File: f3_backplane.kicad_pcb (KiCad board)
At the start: 4 copper layers, 95.8 x 73.8 mm, 47 parts, among them J1 PCIEx4_HOST, J2 Bus_M.2_Socket_M, J3 SATA_Backplane, J4 SATA_Backplane, U1 NCP45521, U2 NCP45521, U3 NCP45521, U4 NCP45521

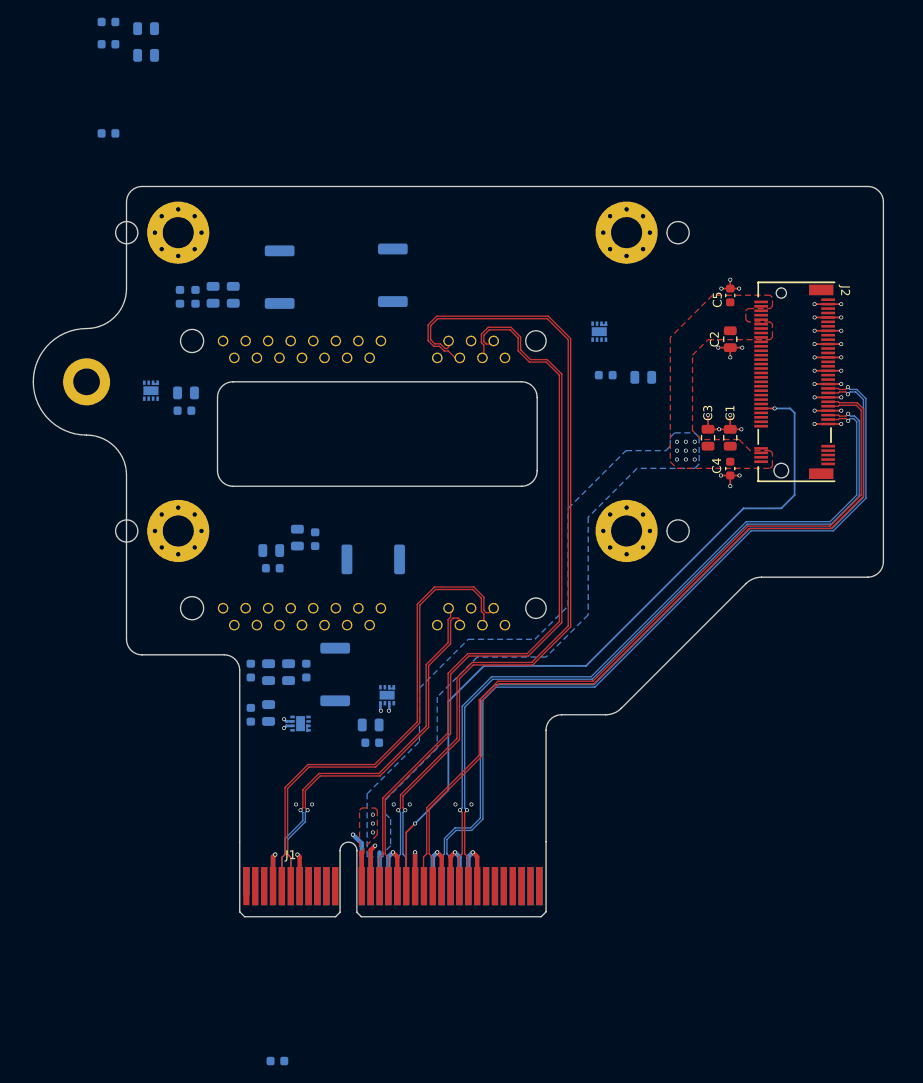
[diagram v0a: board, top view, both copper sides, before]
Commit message: Routing power
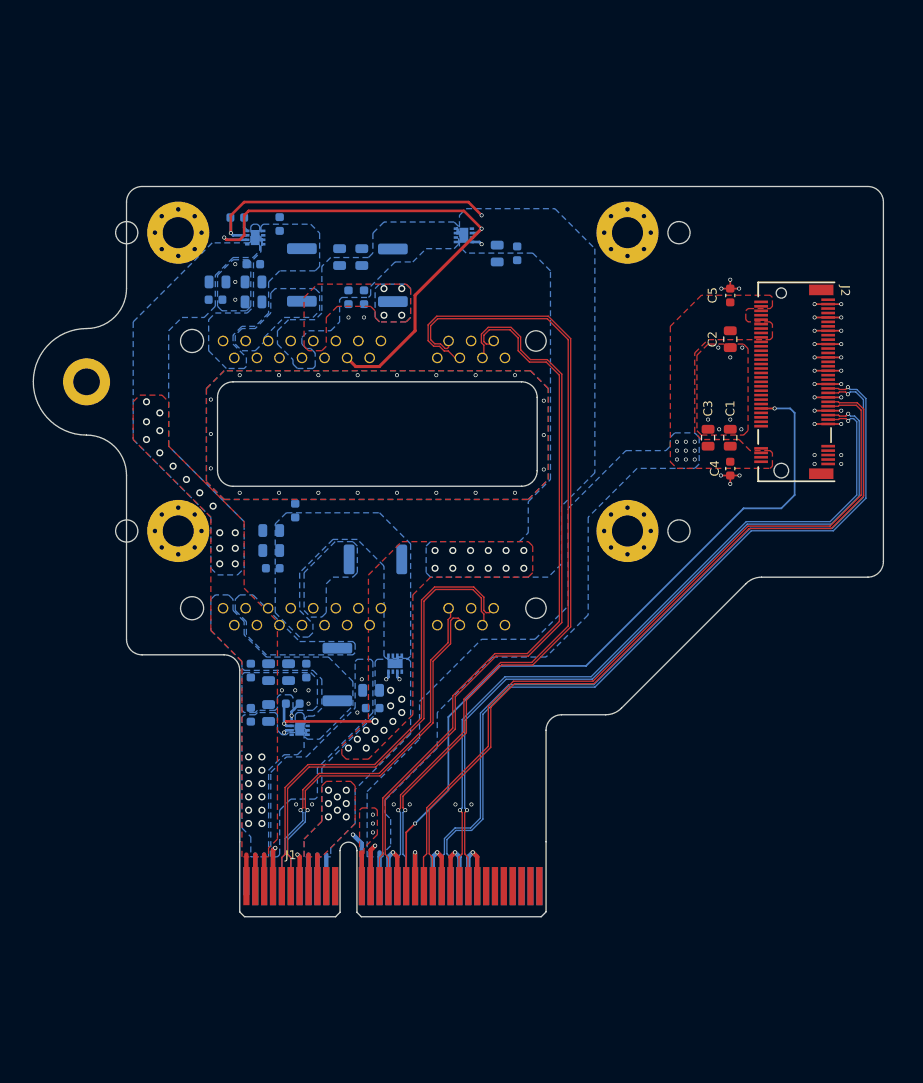
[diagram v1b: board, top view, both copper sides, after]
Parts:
- moved C34 42.3 mm to (139.0, 58.7), turned to -90 degrees
- moved C22 40.3 mm to (131.0, 104.5), turned to 0 degrees
- moved C35 39.3 mm to (137.2, 58.7), turned to -90 degrees
- moved C32 35.4 mm to (138.8, 54.2), turned to 90 degrees
- moved C33 31.5 mm to (136.2, 54.2), turned to 90 degrees
- moved C30 21.6 mm to (154.0, 53.8), turned to -90 degrees
- moved U4 20.9 mm to (126.8, 52.0), turned to 90 degrees
- moved U3 18.7 mm to (150.2, 51.8), turned to -90 degrees
- moved C42 17.3 mm to (124.7, 49.8), turned to 0 degrees
- moved C31 17.0 mm to (156.2, 53.8), turned to -90 degrees
- moved C40 13.9 mm to (129.5, 50.5)
- moved C36 13.0 mm to (122.5, 57.0)
- moved C37 13.0 mm to (122.3, 59.0)
- moved C41 7.47 mm to (126.5, 55.0), turned to 180 degrees
- moved C39 4.78 mm to (126.5, 57.0), turned to 180 degrees
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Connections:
- net Net-(J3-12V_PRE) renamed /SATA1/SATA_PRE_12V
- net Net-(J3-5V_PRE) renamed /SATA1/SATA_PRE_5V
- net Net-(J4-12V_PRE) renamed /SATA2/SATA_PRE_12V
- net Net-(J4-5V_PRE) renamed /SATA2/SATA_PRE_5V
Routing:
- net +5V: track 1.05 -> 66.5 mm, vias 1 -> 35
- net /SATA2/PRESENT#: track 0.00 -> 60.7 mm, vias 0 -> 2
- net /SATA1/PRESENT#: track 1.92 -> 26.2 mm
- net +12V: track 0.00 -> 17.7 mm, vias 0 -> 28
- net GND: track 109.5 -> 105.3 mm, vias 49 -> 88
- net /SATA2_B-: track 97.4 -> 95.6 mm
- net /SATA2_B+: track 95.2 -> 93.4 mm
- net /SATA2_A-: track 85.2 -> 83.5 mm
- net /SATA2_A+: track 83.7 -> 81.9 mm
- net /PCIE_TX-: track 90.1 -> 89.1 mm
- net /PERST#: track 84.6 -> 83.6 mm
- net /PCIE_TX+: track 89.7 -> 88.6 mm
- net /PCIE_RX-: track 92.5 -> 91.6 mm
- net /PCIE_RX+: track 92.0 -> 91.1 mm
- net /PCIE_REFCLK+: track 86.8 -> 85.9 mm
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- added copper zone on B.Cu, net +12V
- added copper zone on F.Cu, net +12V
- added copper zone on B.Cu, net +5V
- added copper zone on F.Cu, net +5V
- added copper zone on B.Cu, net /SATA1/SATA_12V
- added copper zone on B.Cu, net /SATA1/SATA_5V
- added copper zone on B.Cu, net /SATA1/SATA_PRE_12V
- added copper zone on B.Cu, net /SATA1/SATA_PRE_5V
- added copper zone on B.Cu, net /SATA2/SATA_12V
- added copper zone on B.Cu, net /SATA2/SATA_5V
- added copper zone on B.Cu, net /SATA2/SATA_PRE_12V
- added copper zone on B.Cu, net /SATA2/SATA_PRE_5V
- added copper zone on F.Cu, net /SATA2/SATA_PRE_5V
- added copper zone on B.Cu, net GND
- added copper zone on F.Cu, net GND

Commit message: Add ground plane to outer layers
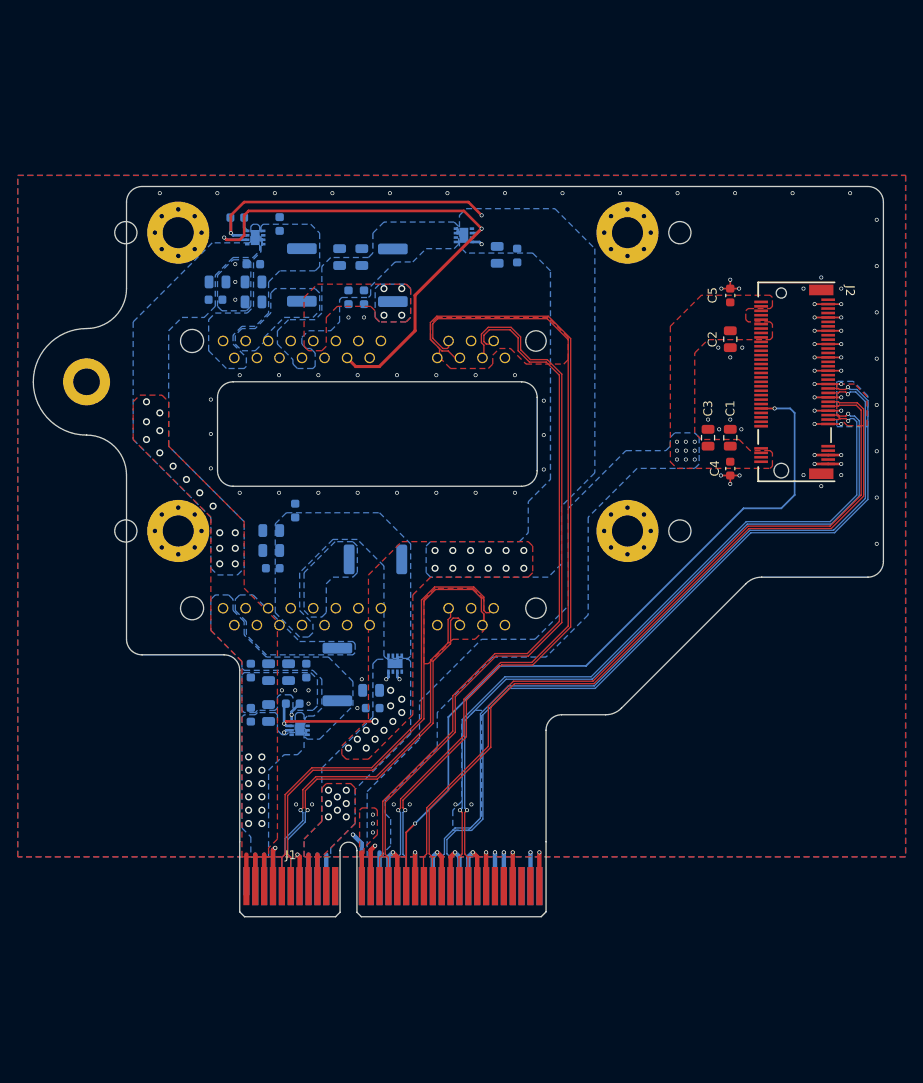
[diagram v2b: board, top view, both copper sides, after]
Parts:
- moved C31 0.25 mm to (156.2, 54.0)
- moved C30 0.15 mm to (154.0, 54.0)
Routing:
- net GND: track 105.3 -> 134.1 mm, vias 88 -> 121

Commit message: Finish v1.0
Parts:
- added C6: 100nF, Capacitor_SMD:C_0603_1608Metric, B.Cu at (156.2, 112.2)
- added G***: LOGO, Logo:f3_logo, F.Cu at (142.2, 111.8)
- added Q1: MMBT3904, Package_TO_SOT_SMD:SOT-23, B.Cu at (156.1, 109.3)
- moved C3 10.9 mm to (179.1, 63.8), turned to 180 degrees
- moved C1 3.28 mm to (179.1, 71.5), turned to 180 degrees
- moved C2 2.51 mm to (179.1, 61.2), turned to 180 degrees
- moved H4 0.36 mm to (169.0, 85.2)
- moved H2 0.30 mm to (169.0, 51.5)
- moved C4 0.25 mm to (180.5, 78.0)
- moved C5 0.25 mm to (180.5, 58.5)
- moved C14 0.25 mm to (131.5, 82.8)
- moved H3 0.22 mm to (118.2, 85.2)
- moved C12 0.20 mm to (128.8, 85.0)
- moved C13 0.20 mm to (128.8, 87.2)
- moved J1 0.16 mm to (125.7, 125.2)
- moved C15 0.15 mm to (128.9, 89.2)
- moved J3 0.15 mm to (139.0, 93.9)
- moved C11 0.10 mm to (139.9, 105.0)
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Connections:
- J1 pad B30: unconnected-(J1-PadB30) -> /Connector/B30
- J1 pad B31: unconnected-(J1-PadB31) -> /Connector/B31
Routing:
- net /Connector/B30: track 0.00 -> 19.0 mm, vias 0 -> 1
- net /Connector/B31: track 0.00 -> 15.4 mm, vias 0 -> 1
- net +3.3V: track 11.4 -> 17.5 mm, vias 12 -> 14
- net GND: track 134.1 -> 128.1 mm, vias 121 -> 142
- net /SATA2_A+: track 81.9 -> 83.5 mm
- net /SATA2_B+: track 92.9 -> 94.1 mm
- net /SATA1_A+: track 53.7 -> 52.5 mm
- net /SATA2_B-: track 95.1 -> 94.2 mm
- net /SATA1_A-: track 53.2 -> 52.3 mm
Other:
- board size 95.8 x 73.8 mm -> 95.8 x 74 mm
- board text added: "JLCJLCJLCJLC"
- board text added: "codedbearder.com"
